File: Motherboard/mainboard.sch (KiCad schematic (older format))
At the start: 45 parts, among them IC1 BMX160, J1 Conn_01x01, J2 10118194-0001LF, J28 Conn_01x01, J29 Conn_01x01, J3 Micro_SD_Card, J30 Conn_01x01, J4 xf2m-2415-1a, J5 XF2M-1015-1A, SW1 KMR231NG LFS, U1 RFM95W-915S2, U2 ATSAMD51G_TQFN48, U3 DRV8848, U4 TPS82740BSIPR, U5 DRV8848, U6 MAX708RESA-T, U8 RFM95W-915S2

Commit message: branching for fabrication clean-up and review
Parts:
- added J?: Conn_01x01, custom-footprints:castellated_small_1side, symbol mainboard-rescue:Conn_01x01-Connector_Generic
- gave numbers to parts that had none: 2
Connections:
- net ~RESET: now also J?.1 (Pin_1)
- net PA04: no longer names the net of U2.9 (PA04/I4/VREFB/AIN4/SERCOM0.0)
- net PA07: no longer names the net of U2.12 (PA07/I7/AIN7/SERCOM0.3)
- net PA21: no longer names the net of U2.30 (PA21/I5/SERCOM3+5.3/I2SDO)
- net PA22: no longer names the net of U2.31 (PA22/I2C/I6/SERCOM3.0+5.1/I2SDI)
- net PA23: no longer names the net of U2.32 (PA23/I2C/I7/SERCOM3.1+5.0/SOF/I2SFS1)
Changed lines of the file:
@@
 Wire Wire Line
 	6950 5500 7100 5500
-Text GLabel 4550 6300 2    50   BiDi ~ 0
-PA21
-Text GLabel 4550 6500 2    50   BiDi ~ 0
-PA22
-Text GLabel 4550 6600 2    50   BiDi ~ 0
-PA23
 Wire Wire Line
 	1450 5600 1350 5600
@@
 Text GLabel 4600 4500 2    50   BiDi ~ 0
 DAC1
-Text GLabel 4600 4400 2    50   BiDi ~ 0
-PA04
-Text GLabel 4600 4700 2    50   BiDi ~ 0
-PA07
 $Comp
 L mainboard-rescue:Conn_01x01-Connector_Generic J28
@@
 	5450 6700 4450 6700
 Wire Wire Line
-	4450 6600 4550 6600
-Wire Wire Line
-	4450 6500 4550 6500
-Wire Wire Line
-	4450 6300 4550 6300
-Wire Wire Line
 	4450 5800 5250 5800
 Wire Wire Line
@@
 	4550 4900 4450 4900
 Wire Wire Line
-	4450 4700 4600 4700
-Wire Wire Line
 	4450 4500 4600 4500
-Wire Wire Line
-	4450 4400 4600 4400
 Wire Wire Line
 	4450 4300 5150 4300
@@
 Connection ~ 750  6950
 $Comp
-L symbols:U.FL-R-SMT-1 J?
+L symbols:U.FL-R-SMT-1 J6
 U 1 1 5DBA79E5
 P 9450 5150
-F 0 "J?" H 9850 5415 50  0000 C CNN
+F 0 "J6" H 9850 5415 50  0000 C CNN
 F 1 "U.FL-R-SMT-1" H 9850 5324 50  0000 C CNN
 F 2 "custom-footprints:U.FL-R-SMT-1" H 10100 5250 50  0001 L CNN
@@
 	9050 5150 8850 5150
 $Comp
-L symbols:U.FL-R-SMT-1 J?
+L symbols:U.FL-R-SMT-1 J7
 U 1 1 5DBBD914
 P 10400 3900
-F 0 "J?" H 10800 4165 50  0000 C CNN
+F 0 "J7" H 10800 4165 50  0000 C CNN
 F 1 "U.FL-R-SMT-1" H 10800 4074 50  0000 C CNN
 F 2 "custom-footprints:U.FL-R-SMT-1" H 11050 4000 50  0001 L CNN
@@
 	10000 3900 9900 3900
 $Comp
-L power:GND #PWR?
+L power:GND #PWR0136
 U 1 1 5DBC73C0
 P 9550 5450
-F 0 "#PWR?" H 9550 5200 50  0001 C CNN
+F 0 "#PWR0136" H 9550 5200 50  0001 C CNN
 F 1 "GND" H 9555 5277 50  0000 C CNN
 F 2 "" H 9550 5450 50  0001 C CNN
@@
 $EndComp
 $Comp
-L power:GND #PWR?
+L power:GND #PWR0137
 U 1 1 5DBC75A7
 P 10500 4200
-F 0 "#PWR?" H 10500 3950 50  0001 C CNN
+F 0 "#PWR0137" H 10500 3950 50  0001 C CNN
 F 1 "GND" H 10505 4027 50  0000 C CNN
 F 2 "" H 10500 4200 50  0001 C CNN
@@
 	1    0    0    -1
 $EndComp
+$Comp
+L mainboard-rescue:Conn_01x01-Connector_Generic J?
+U 1 1 5DC2AE71
+P 4700 7550
+F 0 "J?" V 4800 7450 50  0000 L CNN
+F 1 "Conn_01x01" V 4663 7630 50  0001 L CNN
+F 2 "custom-footprints:castellated_small_1side" H 4700 7550 50  0001 C CNN
+F 3 "~" H 4700 7550 50  0001 C CNN
+F 4 "DNP" H -300 0   50  0001 C CNN "DNP"
+	1    4700 7550
+	0    1    1    0
+$EndComp
+Text GLabel 4650 7350 0    50   BiDi ~ 0
+~RESET
+Wire Wire Line
+	4650 7350 4700 7350
 $EndSCHEMATC

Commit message: placement clean-up
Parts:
- J1, J28, J29, J30: footprint custom-footprints:castellated_small_1side -> TestPoint:TestPoint_Pad_D1.0mm
- J8: renamed from J?; footprint custom-footprints:castellated_small_1side -> TestPoint:TestPoint_Pad_D1.0mm
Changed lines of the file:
@@
 F 0 "J28" V 5100 7450 50  0000 L CNN
 F 1 "Conn_01x01" V 4963 7630 50  0001 L CNN
-F 2 "custom-footprints:castellated_small_1side" H 5000 7550 50  0001 C CNN
+F 2 "TestPoint:TestPoint_Pad_D1.0mm" H 5000 7550 50  0001 C CNN
 F 3 "~" H 5000 7550 50  0001 C CNN
 F 4 "DNP" H 0   0   50  0001 C CNN "DNP"
@@
 F 0 "J1" V 5000 7500 50  0000 L CNN
 F 1 "Conn_01x01" V 4863 7630 50  0001 L CNN
-F 2 "custom-footprints:castellated_small_1side" H 4900 7550 50  0001 C CNN
+F 2 "TestPoint:TestPoint_Pad_D1.0mm" H 4900 7550 50  0001 C CNN
 F 3 "~" H 4900 7550 50  0001 C CNN
 F 4 "DNP" H 0   0   50  0001 C CNN "DNP"
@@
 F 0 "J29" V 4900 7450 50  0000 L CNN
 F 1 "Conn_01x01" V 4763 7630 50  0001 L CNN
-F 2 "custom-footprints:castellated_small_1side" H 4800 7550 50  0001 C CNN
+F 2 "TestPoint:TestPoint_Pad_D1.0mm" H 4800 7550 50  0001 C CNN
 F 3 "~" H 4800 7550 50  0001 C CNN
 F 4 "DNP" H 0   0   50  0001 C CNN "DNP"
@@
 F 0 "J30" V 5200 7500 50  0000 L CNN
 F 1 "Conn_01x01" V 5063 7630 50  0001 L CNN
-F 2 "custom-footprints:castellated_small_1side" H 5100 7550 50  0001 C CNN
+F 2 "TestPoint:TestPoint_Pad_D1.0mm" H 5100 7550 50  0001 C CNN
 F 3 "~" H 5100 7550 50  0001 C CNN
 F 4 "DNP" H 0   0   50  0001 C CNN "DNP"
@@
 $EndComp
 $Comp
-L mainboard-rescue:Conn_01x01-Connector_Generic J?
+L mainboard-rescue:Conn_01x01-Connector_Generic J8
 U 1 1 5DC2AE71
 P 4700 7550
-F 0 "J?" V 4800 7450 50  0000 L CNN
+F 0 "J8" V 4800 7450 50  0000 L CNN
 F 1 "Conn_01x01" V 4663 7630 50  0001 L CNN
-F 2 "custom-footprints:castellated_small_1side" H 4700 7550 50  0001 C CNN
+F 2 "TestPoint:TestPoint_Pad_D1.0mm" H 4700 7550 50  0001 C CNN
 F 3 "~" H 4700 7550 50  0001 C CNN
 F 4 "DNP" H -300 0   50  0001 C CNN "DNP"

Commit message: placement getting closer
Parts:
- added FID1, FID2, FID3, FID4: Fiducial, custom-footprints:Fiducial_1mm_Silkscreen, symbol Mechanical:Fiducial
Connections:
- net DXZ_FAULT: no longer U5.8 (nFAULT)
- net MINX_1: no longer U5.16 (AIN1), U5.2 (AOUT1)
- net MINX_2: no longer U5.15 (AIN2), U5.4 (AOUT2)
- net MINZ_1: no longer U5.9 (BIN1)
- net MINZ_2: no longer U5.10 (BIN2)
- net MOZ_1: no longer U5.7 (BOUT1)
- net MOZ_2: no longer U5.5 (BOUT2)
- net MXZ_EN: no longer U5.1 (nSLEEP)
- net RF2_IO1: now reaches U1.15 (DIO1)
- net CS_RF1 renamed RF1_CS
- net CS_RF2 renamed RF2_CS
- net RF_BUSY: no longer names the net of U2.22 (PA13/I13/I2C/SERCOM2.1+4.0)
- net RF_BUSY: no longer U8.12 (DIO4)
- net RF_CS: no longer names the net of U2.19 (PB10/I10/SERCOM4.2/I2SDI)
- net RF_DIO0: no longer names the net of U2.47 (PB02/I2/AIN14/SERCOM5.0)
- net RF_DIO0: no longer U8.14 (DIO0)
- net RF_DIO1: no longer names the net of U2.39 (PA27/I11)
- net RF_DIO1: no longer U8.15 (DIO1)
- net RF_DIO2: no longer names the net of U2.38 (PB23/I7/SERCOM1+5.3)
- net RF_DIO2: no longer U8.16 (DIO2)
- net RF_DIO3: no longer names the net of U2.23 (PA14/I14/SERCOM2+4.2)
- net RF_DIO3: no longer U8.11 (DIO3)
- net RF_RST: no longer names the net of U2.21 (PA12/I12/I2C/SERCOM2.0+4.1)
- net RF_RST: no longer U8.6 (RESET)
- new net DY_FAULT: U5.8 (nFAULT)
- new net MINY_1: U5.16 (AIN1)
- new net MINY_2: U5.15 (AIN2)
- new net MOY_1: U5.2 (AOUT1)
- new net MOY_2: U5.4 (AOUT2)
- new net MY_EN: U5.1 (nSLEEP)
- new net RF1_BUSY: U8.12 (DIO4)
- new net RF1_IO1: U8.15 (DIO1)
- new net RF1_RST: U8.6 (RESET)
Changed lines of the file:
@@
 Wire Wire Line
 	7750 5350 7850 5350
-Wire Wire Line
-	8850 5650 8950 5650
-Text GLabel 8950 5650 2    50   BiDi ~ 0
-RF_DIO2
 $Comp
 L power:GND #PWR0140
@@
 Wire Wire Line
 	7850 5650 7750 5650
-Text GLabel 7750 5450 0    50   Input ~ 0
-CS_RF1
-Text GLabel 7750 5650 0    50   BiDi ~ 0
-RF_RST
-Text GLabel 8950 5550 2    50   BiDi ~ 0
-RF_DIO3
-Text GLabel 8950 5450 2    50   Output ~ 0
-RF_BUSY
-Text GLabel 8950 5750 2    50   BiDi ~ 0
-RF_DIO1
-Wire Wire Line
-	8950 5550 8850 5550
-Wire Wire Line
-	8950 5750 8850 5750
 Wire Wire Line
 	8950 5450 8850 5450
-Wire Wire Line
-	1450 5800 1350 5800
-Text GLabel 1350 5800 0    50   Input ~ 0
-RF_CS
-Text GLabel 4550 5300 2    50   BiDi ~ 0
-RF_RST
-Wire Wire Line
-	1450 6100 1350 6100
-Text GLabel 1350 6100 0    50   BiDi ~ 0
-RF_DIO2
-Text GLabel 4550 5600 2    50   BiDi ~ 0
-RF_DIO3
-Text GLabel 4550 5400 2    50   Output ~ 0
-RF_BUSY
-Text GLabel 4550 6900 2    50   BiDi ~ 0
-RF_DIO1
-Text GLabel 8950 5850 2    50   BiDi ~ 0
-RF_DIO0
-Wire Wire Line
-	8950 5850 8850 5850
-Text GLabel 1350 5400 0    50   BiDi ~ 0
-RF_DIO0
-Wire Wire Line
-	1350 5400 1450 5400
 Text GLabel 4600 4500 2    50   BiDi ~ 0
 DAC1
@@
 $EndComp
 Wire Wire Line
-	8900 4200 8800 4200
-Wire Wire Line
 	8900 4400 8800 4400
-Text GLabel 8800 4200 0    50   Input ~ 0
-CS_RF2
 Text GLabel 8800 4400 0    50   BiDi ~ 0
 RF2_RST
@@
 P 8400 1050
 F 0 "#PWR0124" H 8400 800 50  0001 C CNN
-F 1 "GND" H 8405 877 50  0000 C CNN
+F 1 "GND" H 8550 1000 50  0000 C CNN
 F 2 "" H 8400 1050 50  0001 C CNN
 F 3 "" H 8400 1050 50  0001 C CNN
@@
 P 8100 1850
 F 0 "#PWR0128" H 8100 1600 50  0001 C CNN
-F 1 "GND" H 8105 1677 50  0000 C CNN
+F 1 "GND" H 8250 1800 50  0000 C CNN
 F 2 "" H 8100 1850 50  0001 C CNN
 F 3 "" H 8100 1850 50  0001 C CNN
@@
 P 8100 2250
 F 0 "#PWR0129" H 8100 2000 50  0001 C CNN
-F 1 "GND" H 8105 2077 50  0000 C CNN
+F 1 "GND" H 8250 2200 50  0000 C CNN
 F 2 "" H 8100 2250 50  0001 C CNN
 F 3 "" H 8100 2250 50  0001 C CNN
@@
 $EndComp
 Text GLabel 8800 1500 0    50   Input ~ 0
-DXZ_FAULT
+DY_FAULT
 Text GLabel 8800 1600 0    50   Input ~ 0
-MXZ_EN
+MY_EN
 Text GLabel 8800 1800 0    50   Input ~ 0
-MINX_1
+MINY_1
 Text GLabel 8800 1900 0    50   Input ~ 0
-MINX_2
-Text GLabel 8800 2100 0    50   Input ~ 0
-MINZ_1
-Text GLabel 8800 2200 0    50   Input ~ 0
-MINZ_2
+MINY_2
 $Comp
 L mainboard-rescue:DRV8848-Driver_Motor U5
@@
 $EndComp
 Text GLabel 10000 1600 2    50   Input ~ 0
-MINX_1
+MOY_1
 Text GLabel 10000 1700 2    50   Input ~ 0
-MINX_2
-Text GLabel 10000 2000 2    50   Input ~ 0
-MOZ_1
-Text GLabel 10000 2100 2    50   Input ~ 0
-MOZ_2
+MOY_2
 Wire Wire Line
 	9400 2500 9400 2400
@@
 P 10000 1800
 F 0 "#PWR0132" H 10000 1550 50  0001 C CNN
-F 1 "GND" H 10005 1627 50  0000 C CNN
+F 1 "GND" H 10150 1750 50  0000 C CNN
 F 2 "" H 10000 1800 50  0001 C CNN
 F 3 "" H 10000 1800 50  0001 C CNN
@@
 	1    0    0    -1
 $EndComp
-Wire Wire Line
-	10000 1850 10000 1800
 $Comp
 L power:GND #PWR0133
@@
 P 10000 2200
 F 0 "#PWR0133" H 10000 1950 50  0001 C CNN
-F 1 "GND" H 10005 2027 50  0000 C CNN
+F 1 "GND" H 10150 2150 50  0000 C CNN
 F 2 "" H 10000 2200 50  0001 C CNN
 F 3 "" H 10000 2200 50  0001 C CNN
@@
 	1    0    0    -1
 $EndComp
-Wire Wire Line
-	10000 2250 10000 2200
-Connection ~ 10000 1800
-Connection ~ 10000 2200
 Text GLabel 5950 3250 2    50   Output ~ 0
 MOSI
@@
 	4450 7100 5000 7100
 Wire Wire Line
-	4550 6900 4450 6900
-Wire Wire Line
 	5450 6800 4450 6800
 Wire Wire Line
@@
 	4450 5800 5250 5800
 Wire Wire Line
-	4450 5300 4550 5300
-Wire Wire Line
 	4550 5100 4450 5100
 Wire Wire Line
@@
 Wire Wire Line
 	4450 4200 4600 4200
-Wire Wire Line
-	4550 5600 4450 5600
-Wire Wire Line
-	4550 5400 4450 5400
 Wire Wire Line
 	5300 5900 5100 5900
@@
 Wire Wire Line
 	4650 7350 4700 7350
+Text GLabel -1750 5200 0    50   Input ~ 0
+DXZ_FAULT
+Text GLabel -1750 5300 0    50   Input ~ 0
+MXZ_EN
+Text GLabel -1750 5500 0    50   Input ~ 0
+MINX_1
+Text GLabel -1750 5600 0    50   Input ~ 0
+MINX_2
+Text GLabel -1750 5800 0    50   Input ~ 0
+MINZ_1
+Text GLabel -1750 5900 0    50   Input ~ 0
+MINZ_2
+Text GLabel -1250 5200 0    50   Input ~ 0
+DY_FAULT
+Text GLabel -1250 5300 0    50   Input ~ 0
+MY_EN
+Text GLabel -1250 5500 0    50   Input ~ 0
+MINY_1
+Text GLabel -1250 5600 0    50   Input ~ 0
+MINY_2
+$Comp
+L Mechanical:Fiducial FID1
+U 1 1 5DB69FCA
+P 9700 6050
+F 0 "FID1" H 9785 6096 50  0000 L CNN
+F 1 "Fiducial" H 9785 6005 50  0000 L CNN
+F 2 "custom-footprints:Fiducial_1mm_Silkscreen" H 9700 6050 50  0001 C CNN
+F 3 "~" H 9700 6050 50  0001 C CNN
+	1    9700 6050
+	1    0    0    -1
+$EndComp
+$Comp
+L Mechanical:Fiducial FID2
+U 1 1 5DB71FBE
+P 9700 6250
+F 0 "FID2" H 9785 6296 50  0000 L CNN
+F 1 "Fiducial" H 9785 6205 50  0000 L CNN
+F 2 "custom-footprints:Fiducial_1mm_Silkscreen" H 9700 6250 50  0001 C CNN
+F 3 "~" H 9700 6250 50  0001 C CNN
+	1    9700 6250
+	1    0    0    -1
+$EndComp
+$Comp
+L Mechanical:Fiducial FID3
+U 1 1 5DB7214D
+P 9700 6450
+F 0 "FID3" H 9785 6496 50  0000 L CNN
+F 1 "Fiducial" H 9785 6405 50  0000 L CNN
+F 2 "custom-footprints:Fiducial_1mm_Silkscreen" H 9700 6450 50  0001 C CNN
+F 3 "~" H 9700 6450 50  0001 C CNN
+	1    9700 6450
+	1    0    0    -1
+$EndComp
+$Comp
+L Mechanical:Fiducial FID4
+U 1 1 5DB722FE
+P 9700 6650
+F 0 "FID4" H 9785 6696 50  0000 L CNN
+F 1 "Fiducial" H 9785 6605 50  0000 L CNN
+F 2 "custom-footprints:Fiducial_1mm_Silkscreen" H 9700 6650 50  0001 C CNN
+F 3 "~" H 9700 6650 50  0001 C CNN
+	1    9700 6650
+	1    0    0    -1
+$EndComp
+Text GLabel -2050 6450 2    50   BiDi ~ 0
+RF1_BUSY
+Text GLabel -2050 6550 2    50   BiDi ~ 0
+RF1_RST
+Text GLabel -2050 6650 2    50   BiDi ~ 0
+RF1_CS
+Text GLabel -1550 6450 2    50   BiDi ~ 0
+RF1_IO1
+Text GLabel 8800 4200 0    50   BiDi ~ 0
+RF2_CS
+Wire Wire Line
+	8800 4200 8900 4200
+Text GLabel -2050 6100 2    50   BiDi ~ 0
+RF2_CS
+Text GLabel -1550 6300 2    50   BiDi ~ 0
+RF2_IO1
+Text GLabel -2050 6200 2    50   BiDi ~ 0
+RF2_RST
+Text GLabel -2050 6300 2    50   BiDi ~ 0
+RF2_BUSY
+Text GLabel 10000 4500 2    50   BiDi ~ 0
+RF2_IO1
+Wire Wire Line
+	10000 4500 9900 4500
+Text GLabel 8950 5450 2    50   BiDi ~ 0
+RF1_BUSY
+Text GLabel 7750 5650 0    50   BiDi ~ 0
+RF1_RST
+Text GLabel 7750 5450 0    50   BiDi ~ 0
+RF1_CS
+Text GLabel 8950 5750 2    50   BiDi ~ 0
+RF1_IO1
+Wire Wire Line
+	8950 5750 8850 5750
 $EndSCHEMATC

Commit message: placement roughed-in & routing planned
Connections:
- net CS_CAM: no longer U2.24 (PA15/I15/SERCOM2+4.3)
- net CS_IMU: no longer U2.27 (PA18/I2/SERCOM1+3.2)
- net EN_CAM: no longer U2.29 (PA20/I4/SERCOM3+5.2/I2SFS0)
- net SCL2: now also J4.2; no longer J4.1
- net SDA2: now also J4.1; no longer J4.2
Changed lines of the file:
@@
 Text GLabel 5950 3050 2    50   Input ~ 0
 BATT_N
-Text GLabel 4550 5700 2    50   Input ~ 0
+Text GLabel -1100 4600 2    50   Input ~ 0
 CS_CAM
 Connection ~ 1450 7000
@@
 	1    0    0    -1
 $EndComp
-Text GLabel 4550 6200 2    50   Input ~ 0
+Text GLabel -1050 4400 2    50   Input ~ 0
 EN_CAM
 Text GLabel 5300 5800 2    59   BiDi ~ 0
@@
 Text GLabel 4700 4100 2    59   BiDi ~ 0
 SCL1
-Wire Wire Line
-	4550 5700 4450 5700
 Text Notes 1650 7550 0    50   ~ 0
 UART:\nTX: PB08\nRX: PB09\n
@@
 Text GLabel 5200 1950 0    59   BiDi ~ 0
 SCL1
+Text GLabel 6100 1250 2    59   BiDi ~ 0
+SCL2
 Text GLabel 5200 1250 0    59   BiDi ~ 0
-SCL2
-Text GLabel 6100 1250 2    59   BiDi ~ 0
 SDA2
-Wire Wire Line
-	4550 6200 4450 6200
 $Comp
 L mainboard-rescue:R_US-Device R4
@@
 Wire Wire Line
 	5250 5800 5300 5800
-Text GLabel 4450 6000 2    50   Output ~ 0
-CS_IMU
 $Comp
 L mainboard-rescue:XF2M-1015-1A-symbols J5
@@
 Text GLabel -1250 5300 0    50   Input ~ 0
 MY_EN
-Text GLabel -1250 5500 0    50   Input ~ 0
+Text GLabel -1800 4850 2    50   Input ~ 0
 MINY_1
-Text GLabel -1250 5600 0    50   Input ~ 0
+Text GLabel -1800 4950 2    50   Input ~ 0
 MINY_2
 $Comp
@@
 Wire Wire Line
 	8950 5750 8850 5750
+Text GLabel -1100 4850 2    50   Output ~ 0
+CS_IMU
 $EndSCHEMATC

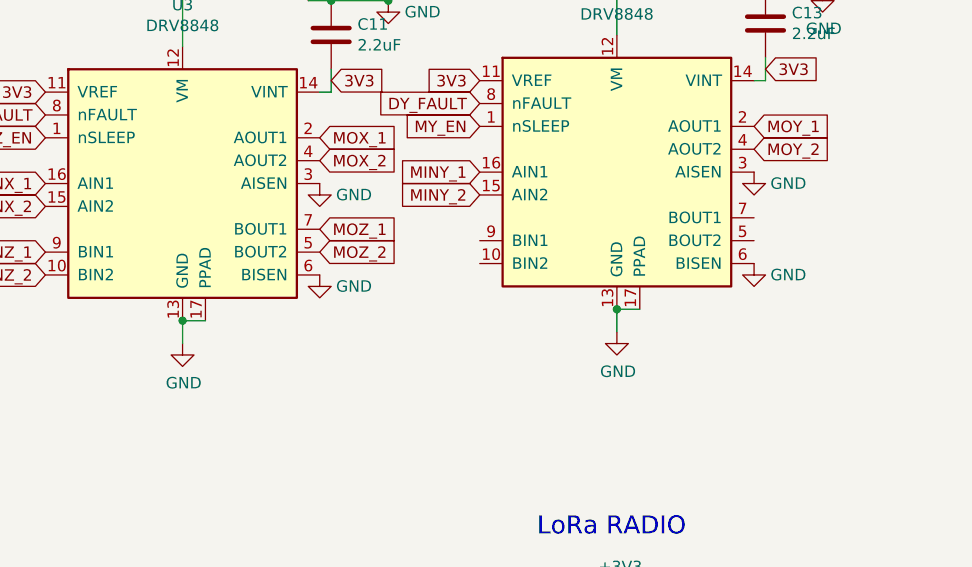
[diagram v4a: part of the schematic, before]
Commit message: rearranging for power distrobution
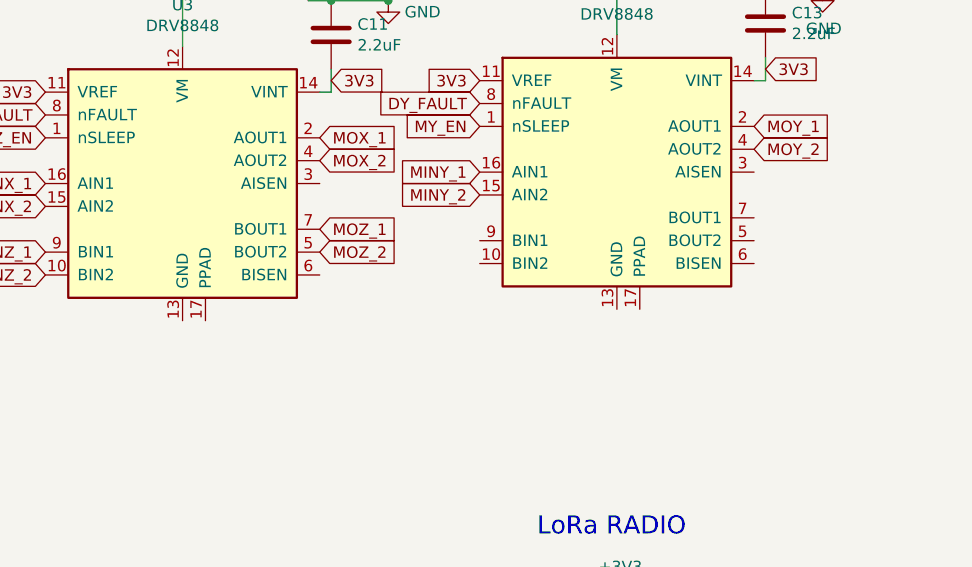
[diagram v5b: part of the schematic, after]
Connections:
- net GND: no longer U3.13 (GND), U3.17 (PPAD), U3.3 (AISEN), U3.6 (BISEN), U5.13 (GND), U5.17 (PPAD), U5.3 (AISEN), U5.6 (BISEN)
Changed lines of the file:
@@
 Wire Wire Line
 	7500 750  8050 750
-$Comp
-L power:GND #PWR0125
-U 1 1 5DC582A1
-P 7500 2550
-F 0 "#PWR0125" H 7500 2300 50  0001 C CNN
-F 1 "GND" H 7505 2377 50  0000 C CNN
-F 2 "" H 7500 2550 50  0001 C CNN
-F 3 "" H 7500 2550 50  0001 C CNN
-	1    7500 2550
-	1    0    0    -1
-$EndComp
 Text GLabel 6900 1550 0    50   Input ~ 0
 DXZ_FAULT
@@
 Text GLabel 8100 2150 2    50   Input ~ 0
 MOZ_2
-Wire Wire Line
-	7500 2550 7500 2450
-Wire Wire Line
-	7600 2450 7500 2450
-Connection ~ 7500 2450
-$Comp
-L power:GND #PWR0128
-U 1 1 5DCE2BBF
-P 8100 1850
-F 0 "#PWR0128" H 8100 1600 50  0001 C CNN
-F 1 "GND" H 8250 1800 50  0000 C CNN
-F 2 "" H 8100 1850 50  0001 C CNN
-F 3 "" H 8100 1850 50  0001 C CNN
-	1    8100 1850
-	1    0    0    -1
-$EndComp
-$Comp
-L power:GND #PWR0129
-U 1 1 5DCE9737
-P 8100 2250
-F 0 "#PWR0129" H 8100 2000 50  0001 C CNN
-F 1 "GND" H 8250 2200 50  0000 C CNN
-F 2 "" H 8100 2250 50  0001 C CNN
-F 3 "" H 8100 2250 50  0001 C CNN
-	1    8100 2250
-	1    0    0    -1
-$EndComp
 $Comp
 L mainboard-rescue:C-Device C12
@@
 Wire Wire Line
 	9400 700  9950 700
-$Comp
-L power:GND #PWR0131
-U 1 1 5DD0AED6
-P 9400 2500
-F 0 "#PWR0131" H 9400 2250 50  0001 C CNN
-F 1 "GND" H 9405 2327 50  0000 C CNN
-F 2 "" H 9400 2500 50  0001 C CNN
-F 3 "" H 9400 2500 50  0001 C CNN
-	1    9400 2500
-	1    0    0    -1
-$EndComp
 Text GLabel 8800 1500 0    50   Input ~ 0
 DY_FAULT
@@
 Text GLabel 10000 1700 2    50   Input ~ 0
 MOY_2
-Wire Wire Line
-	9400 2500 9400 2400
-Wire Wire Line
-	9500 2400 9400 2400
-Connection ~ 9400 2400
-$Comp
-L power:GND #PWR0132
-U 1 1 5DD0AEF2
-P 10000 1800
-F 0 "#PWR0132" H 10000 1550 50  0001 C CNN
-F 1 "GND" H 10150 1750 50  0000 C CNN
-F 2 "" H 10000 1800 50  0001 C CNN
-F 3 "" H 10000 1800 50  0001 C CNN
-	1    10000 1800
-	1    0    0    -1
-$EndComp
-$Comp
-L power:GND #PWR0133
-U 1 1 5DD0AEF9
-P 10000 2200
-F 0 "#PWR0133" H 10000 1950 50  0001 C CNN
-F 1 "GND" H 10150 2150 50  0000 C CNN
-F 2 "" H 10000 2200 50  0001 C CNN
-F 3 "" H 10000 2200 50  0001 C CNN
-	1    10000 2200
-	1    0    0    -1
-$EndComp
 Text GLabel 5950 3250 2    50   Output ~ 0
 MOSI
